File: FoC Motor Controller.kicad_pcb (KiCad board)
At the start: 6 copper layers, 80 x 93.5 mm, 259 parts, among them J1 XT60PW-F, J10 JST_2mm_LiPo, J11 Conn_ARM_SWD_TagConnect_TC203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, J2 XT60PW-M, J3 SM07B-GHS-TB, J6 Conn_01x03, J7 1054301103, J8 1054301103, J9 USB_C_Receptacle_USB2.0_16P, Q1 IPT015N10N5, Q2 IPT015N10N5, Q3 IPT015N10N5, Q4 IPT015N10N5, Q5 IPT015N10N5, Q6 IPT015N10N5, Q7 AO3404A, Q8 AO3404A, SW1 SW_Push_DPDT, U1 LMR38010FDDAR, U2 NCP176AMX330TCG, U3 TPS62172DSG, U4 STM32G431CBT6, U5 DRV8323SRTAR, U6 AS5047P-ATSM, U7 CH340X, U8 TCAN1051HVDR, Y1 CSTNE8M00G520000R0

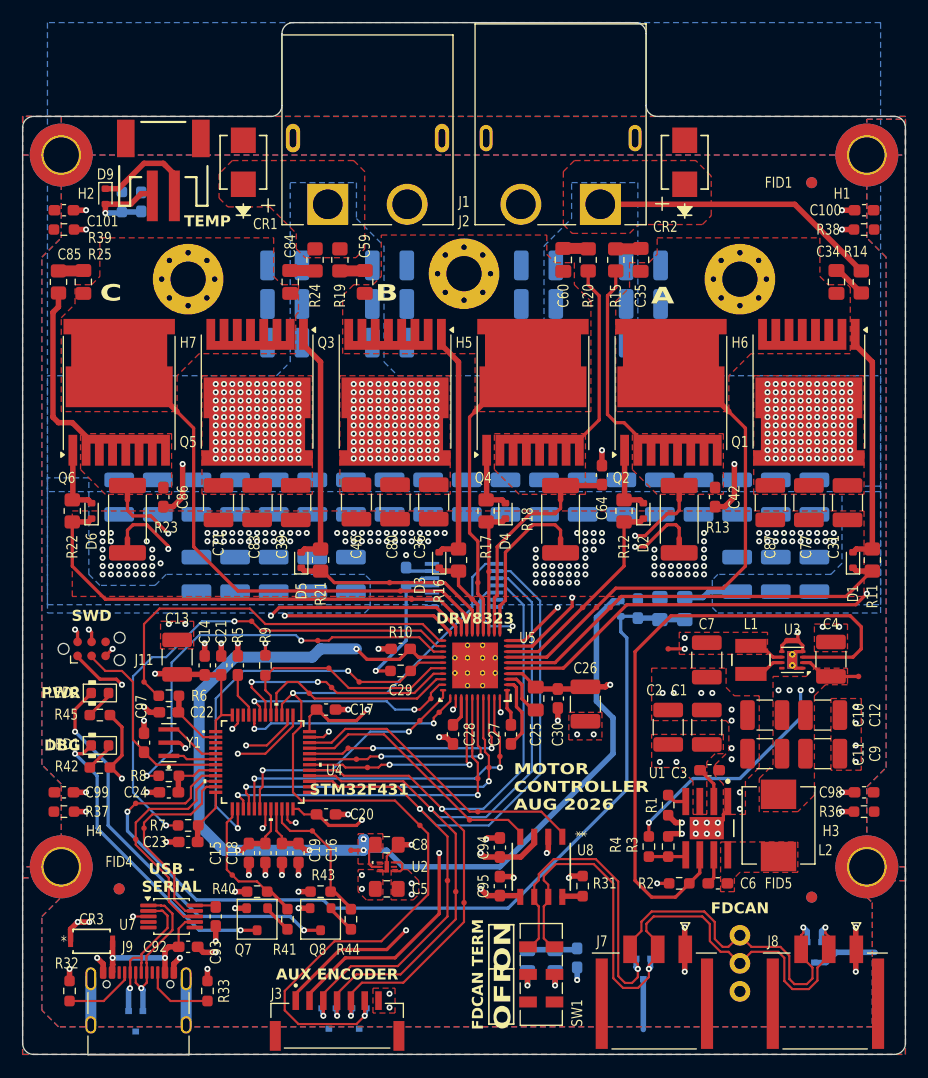
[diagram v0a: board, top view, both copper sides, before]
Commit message: Reorganize project into Altium-style folder structure; add README
- Move hierarchical sheets to Schematics/, lib/ -> Libraries/,
  Manufacturing/ -> Project Outputs/ (BOM, Assembly, Netlist,
  Fabrication, PDF), LTspice benches -> Simulation/
- Update Sheetfile, ${KIPRJMOD} library/3D-model, and output paths
- Drop unused sheets, datasheets, templates and KiCad local history
  from the tracked tree (kept locally, now in .gitignore)
- README.md is the design build log

Co-Authored-By: Claude Sonnet 5 <noreply@anthropic.com>
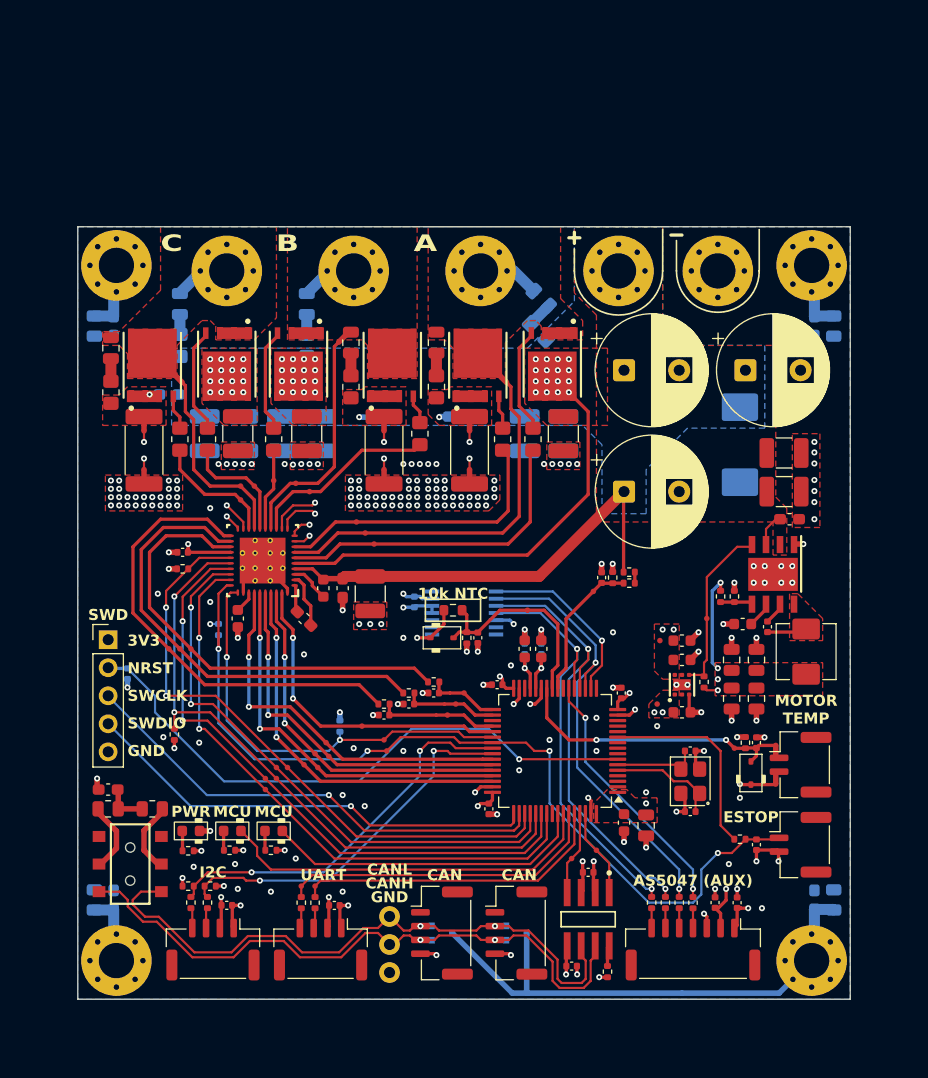
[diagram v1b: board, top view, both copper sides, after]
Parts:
- removed C100, C101: 1n X7R 1kV, Capacitor_SMD:C_0603_1608Metric_Pad1.08x0.95mm_HandSolder
- removed the C13 at (127.5, 89.0)
- removed the C14 at (130.0, 89.8)
- removed the C25 at (160.0, 92.8)
- removed the C26 at (164.5, 93.2)
- removed the C32 at (174.8, 74.5)
- removed the C33 at (178.2, 74.5)
- removed the C4 at (186.8, 89.2)
- removed the C5 at (146.5, 110.0)
- removed C53, C54, C55, C63, C69, C71, C82, C83, C87: 10u X7R 100V, Capacitor_SMD:C_1210_3225Metric_Pad1.33x2.70mm_HandSolder
- removed the C60 at (162.5, 53.0)
- removed C64, C86, C88, C90, C91, C92, C93, C94: 100n X7R 100V, Capacitor_SMD:C_0603_1608Metric_Pad1.08x0.95mm_HandSolder
- removed the C65 at (160.2, 53.5)
- removed the C67 at (137.2, 57.0)
- removed the C68 at (160.8, 74.5)
- removed the C73 at (178.2, 81.5)
- removed the C74 at (157.2, 74.5)
- removed C8: 1u X7R 25V, Capacitor_SMD:C_0805_2012Metric_Pad1.18x1.45mm_HandSolder
- removed C84, C85: 2n2 X7R 100V, Capacitor_SMD:C_0805_2012Metric_Pad1.18x1.45mm_HandSolder
- removed CR1, CR2: SMBJ58CA, SMBJ58CA:SMB
- removed CR3: SM5817PL-TP, SM5817PL-TP:CR_5817PL-TP_MCC
- removed D11, D13, D14: PESD2CANFD24V-UX, PESD2CANFD24V-UX:TVS_PESD2CANFD24V-UX
- removed D2, D3, D5, D6, D8, D9: 1N4148WT, Diode_SMD:D_SOD-523
- removed the D4 at (157.2, 75.8)
- removed the D7 at (167.7, 84.6)
- removed FID1, FID2, FID3, FID4, FID5, FID6: Fiducial, Fiducial:Fiducial_1mm_Mask3mm
- removed the H5 at (153.5, 54.2)
- removed the H6 at (178.5, 54.8)
- removed the H7 at (128.5, 54.8)
- removed the J2 at (162.2, 42.0)
- removed J8: 1054301103, Nano_Fit_1054301103:MOLEX_1054301103
- removed J9: USB_C_Receptacle_USB2.0_16P, Connector_USB:USB_C_Receptacle_XKB_U262-16XN-4BVC11
- removed L1: 2u2, XFL3012-222MEC:IND_XFL3012_COC
- removed LED2: LED_0603_Green, PCM_LED_SMD_AKL:LED_0603_1608Metric
- removed the NT1 at (183.2, 87.5)
- removed NT12, NT13: NetTie_2, NetTie:NetTie-2_SMD_Pad0.5mm
- removed the NT4 at (177.1, 66.4)
- removed the NT7 at (154.9, 66.4)
- removed Q1, Q2: IPT015N10N5, Package_TO_SOT_SMD:Infineon_PG-HSOF-8-1
- removed R1: 64.9k 1%, Resistor_SMD:R_0603_1608Metric_Pad0.98x0.95mm_HandSolder
- removed the R11 at (190.5, 80.2)
- removed the R12 at (168.0, 75.8)
- removed the R14 at (189.5, 55.0)
- removed the R15 at (167.2, 53.0)
- removed the R17 at (155.5, 75.8)
- removed the R22 at (118.0, 75.8)
- removed the R32 at (117.8, 119.3)
- removed the R40 at (134.8, 110.2)
- removed R43: 100k 1%, Resistor_SMD:R_0603_1608Metric_Pad0.98x0.95mm_HandSolder
- removed R5: 10k 1%, Capacitor_SMD:C_0603_1608Metric_Pad1.08x0.95mm_HandSolder
- removed TP1, TP10, TP2, TP3, TP4, TP5, TP8: TestPoint, PCM_SparkFun-Connector:TestPoint-0.5mm
- removed U2: NCP176AMX330TCG, NCP176AMX330TCG:XDFN6_711AT_ONS
- removed U4: STM32G431CBT6, stm32g431cbt6:LQFP48-7x7mm
- removed the U6 at (153.5, 82.5)
- removed Y1: CSTNE8M00G520000R0, CSTNE8M00G520000R0:OSC_CSTNE8M00G520000R0
- added C10: 1u X5R 25V, Capacitor_SMD:C_0603_1608Metric, F.Cu at (173.2, 87.5)
- added C22: 100n X7R 50V, Capacitor_SMD:C_0402_1005Metric, B.Cu at (159.0, 88.2)
- added C23: 100n X7R 50V, Capacitor_SMD:C_0402_1005Metric, F.Cu at (155.8, 102.8)
- added C24: 1u X5R 25V, Capacitor_SMD:C_0603_1608Metric, F.Cu at (168.0, 104.0)
- added C29: 12pF 50V C0G, Capacitor_SMD:C_0402_1005Metric, F.Cu at (174.0, 103.0)
- added DZ2: MM3Z3V3ST, PCM_Diode_SMD_AKL:D_SOD-323, F.Cu at (151.5, 87.2)
- added DZ3: MM3Z3V3ST, PCM_Diode_SMD_AKL:D_SOD-323, F.Cu at (179.5, 99.5)
- added H1: Phase, MountingHole:MountingHole_3.2mm_M3_Pad_Via, F.Cu at (155.0, 54.0)
- added H2: Phase, MountingHole:MountingHole_3.2mm_M3_Pad_Via, F.Cu at (143.5, 54.0)
- added H3: Phase, MountingHole:MountingHole_3.2mm_M3_Pad_Via, F.Cu at (132.0, 54.0)
- added H8: Power, MountingHole:MountingHole_3.2mm_M3_Pad_Via, F.Cu at (167.5, 54.0)
- added H9: Power, MountingHole:MountingHole_3.2mm_M3_Pad_Via, F.Cu at (176.5, 54.0)
- added J4: Conn_01x04_MountingPin, Connector_JST:JST_GH_BM04B-GHS-TBT_1x04-1MP_P1.25mm_Vertical, F.Cu at (151.5, 114.0)
- added J5: Conn_01x04_MountingPin, Connector_JST:JST_GH_BM04B-GHS-TBT_1x04-1MP_P1.25mm_Vertical, F.Cu at (158.2, 114.0)
- added J6: Conn_01x07_MountingPin, Connector_JST:JST_GH_BM07B-GHS-TBT_1x07-1MP_P1.25mm_Vertical, F.Cu at (174.2, 115.5)
- added LED3: LED_0603_Amber, PCM_LED_SMD_AKL:LED_0603_1608Metric, F.Cu at (136.2, 104.8)
- added LED4: LED_0603_Amber, PCM_LED_SMD_AKL:LED_0603_1608Metric, F.Cu at (128.8, 104.8)
- added NT3: NetTie_2, NetTie:NetTie-2_SMD_Pad0.5mm, F.Cu at (157.0, 63.8)
- added NT6: NetTie_2, NetTie:NetTie-2_SMD_Pad0.5mm, F.Cu at (142.5, 60.1)
- added NT9: NetTie_2, NetTie:NetTie-2_SMD_Pad0.5mm, F.Cu at (127.6, 63.8)
- added R23: 3R9 1% 1/8W, Resistor_SMD:R_0805_2012Metric_Pad1.20x1.40mm_HandSolder, B.Cu at (160.2, 59.5)
- added R31: 0R 1% 1/8W, Resistor_SMD:R_0805_2012Metric_Pad1.20x1.40mm_HandSolder, F.Cu at (127.8, 69.2)
- added R34: 3R9 1% 1/8W, Resistor_SMD:R_0805_2012Metric_Pad1.20x1.40mm_HandSolder, F.Cu at (121.5, 65.0)
- added R37: 10k NTC, PCM_SparkFun-Resistor:R_0603_1608Metric, F.Cu at (152.5, 84.8)
- added R42: 2k 1%, Resistor_SMD:R_0402_1005Metric, F.Cu at (130.5, 109.8)
- added R47: 100R 1%, Resistor_SMD:R_0402_1005Metric, F.Cu at (174.2, 111.2)
- added R48: 100R 1%, Resistor_SMD:R_0402_1005Metric, F.Cu at (130.2, 111.2)
- added R49: 100R 1%, Resistor_SMD:R_0402_1005Metric, F.Cu at (173.0, 111.2)
- added R50: 100R 1%, Resistor_SMD:R_0402_1005Metric, F.Cu at (128.8, 111.2)
- added R51: 100R 1%, Resistor_SMD:R_0402_1005Metric, F.Cu at (171.8, 111.2)
- added R52: 100R 1%, Resistor_SMD:R_0402_1005Metric, F.Cu at (140.0, 111.2)
- added R53: 100R 1%, Resistor_SMD:R_0402_1005Metric, F.Cu at (170.5, 111.2)
- added R54: 100R 1%, Resistor_SMD:R_0402_1005Metric, F.Cu at (138.8, 111.2)
- added R58: 0R 1% 1/8W, Resistor_SMD:R_0805_2012Metric, B.Cu at (187.0, 111.0)
- added R59: 0R 1% 1/8W, Resistor_SMD:R_0805_2012Metric, B.Cu at (120.0, 111.0)
- added R66: 1k 1%, Resistor_SMD:R_0402_1005Metric, F.Cu at (128.5, 106.5)
- added R72: 24.9k 1%, Resistor_SMD:R_0402_1005Metric, F.Cu at (168.5, 81.3)
- added R73: 12.4k 1%, Resistor_SMD:R_0402_1005Metric, F.Cu at (168.5, 82.3)
- added TP40: TestPoint, PCM_SparkFun-Connector:TestPoint-0.5mm, F.Cu at (136.2, 73.0)
- added TP41: TestPoint, PCM_SparkFun-Connector:TestPoint-0.5mm, F.Cu at (138.2, 73.2)
- added TP42: TestPoint, PCM_SparkFun-Connector:TestPoint-0.5mm, F.Cu at (139.5, 74.0)
- added TP43: TestPoint, PCM_SparkFun-Connector:TestPoint-0.5mm, F.Cu at (134.5, 73.5)
- added TP44: TestPoint, PCM_SparkFun-Connector:TestPoint-0.5mm, F.Cu at (133.2, 73.5)
- added TP45: TestPoint, PCM_SparkFun-Connector:TestPoint-0.5mm, F.Cu at (133.2, 74.8)
- added U5: STM32G431RBTx, Package_QFP:LQFP-64_10x10mm_P0.5mm, F.Cu at (161.8, 97.5)
- added X1: SMD3225-4, PCM_Crystal_AKL:Crystal_SMD_3225-4Pin_3.2x2.5mm, F.Cu at (174.0, 100.2)
- C11: renamed from C9; value 22u X7R 25V -> 22u X5R 16V; footprint Capacitor_SMD:C_1210_3225Metric_Pad1.33x2.70mm_HandSolder -> Capacitor_SMD:C_0805_2012Metric
- C12: renamed from C10; value 22u X7R 25V -> 22u X5R 16V; footprint Capacitor_SMD:C_1210_3225Metric_Pad1.33x2.70mm_HandSolder -> Capacitor_SMD:C_0805_2012Metric
- C13: renamed from C11; value 22u X7R 25V -> 22u X5R 16V; footprint Capacitor_SMD:C_1210_3225Metric_Pad1.33x2.70mm_HandSolder -> Capacitor_SMD:C_0805_2012Metric
- C14: renamed from C12; value 22u X7R 25V -> 22u X5R 16V; footprint Capacitor_SMD:C_1210_3225Metric_Pad1.33x2.70mm_HandSolder -> Capacitor_SMD:C_0805_2012Metric
- C15, C20: value 1u X7R 25V -> 1u X5R 25V; footprint Capacitor_SMD:C_0603_1608Metric_Pad1.08x0.95mm_HandSolder -> Capacitor_SMD:C_0603_1608Metric
- C16: value 1u X7R 25V -> 22u X5R 16V; footprint Capacitor_SMD:C_0603_1608Metric_Pad1.08x0.95mm_HandSolder -> Capacitor_SMD:C_0805_2012Metric
- C17: value 100n X7R 100V -> 1u X5R 25V; footprint Capacitor_SMD:C_0603_1608Metric_Pad1.08x0.95mm_HandSolder -> Capacitor_SMD:C_0603_1608Metric
- C18, C21: value 100n X7R 100V -> 100n X7R 50V; footprint Capacitor_SMD:C_0603_1608Metric_Pad1.08x0.95mm_HandSolder -> Capacitor_SMD:C_0402_1005Metric
- C19: value 100n X7R 100V -> 100n X7R 50V; footprint Capacitor_SMD:C_0603_1608Metric_Pad1.08x0.95mm_HandSolder -> Capacitor_SMD:C_0402_1005Metric; moved to B.Cu
- C25: renamed from C22; value 2n2 X7R 100V -> 2n2 X7R 50V; footprint Capacitor_SMD:C_0603_1608Metric_Pad1.08x0.95mm_HandSolder -> Capacitor_SMD:C_0402_1005Metric
- C26: renamed from C23; value 2n2 X7R 100V -> 2n2 X7R 50V; footprint Capacitor_SMD:C_0603_1608Metric_Pad1.08x0.95mm_HandSolder -> Capacitor_SMD:C_0402_1005Metric
- C27: renamed from C24; value 2n2 X7R 100V -> 2n2 X7R 50V; footprint Capacitor_SMD:C_0603_1608Metric_Pad1.08x0.95mm_HandSolder -> Capacitor_SMD:C_0402_1005Metric
- C28: value 1u X7R 6V3 -> 12pF 50V C0G; footprint Capacitor_SMD:C_0603_1608Metric_Pad1.08x0.95mm_HandSolder -> Capacitor_SMD:C_0402_1005Metric
- C31: value 10u X7R 100V -> 1u X5R 25V; footprint Capacitor_SMD:C_1210_3225Metric_Pad1.33x2.70mm_HandSolder -> Capacitor_SMD:C_0603_1608Metric
- C32: renamed from C29; value 100n X7R 100V -> 100n X7R 50V; footprint Capacitor_SMD:C_0603_1608Metric_Pad1.08x0.95mm_HandSolder -> Capacitor_SMD:C_0402_1005Metric
- C34: value 2n2 X7R 100V -> 100uF 100V; footprint Capacitor_SMD:C_0805_2012Metric_Pad1.18x1.45mm_HandSolder -> Capacitor_THT:CP_Radial_D10.0mm_P5.00mm
- C35: footprint Capacitor_SMD:C_0805_2012Metric_Pad1.18x1.45mm_HandSolder -> Capacitor_SMD:C_0805_2012Metric; moved to B.Cu
- C36, C45, C46, C56: value 10u X7R 100V -> 2n2 X7R 100V; footprint Capacitor_SMD:C_1210_3225Metric_Pad1.33x2.70mm_HandSolder -> Capacitor_SMD:C_0805_2012Metric
- C37: value 10u X7R 100V -> 100uF 100V; footprint Capacitor_SMD:C_1210_3225Metric_Pad1.33x2.70mm_HandSolder -> Capacitor_THT:CP_Radial_D10.0mm_P5.00mm; moved to F.Cu
- C38, C49, C58: value 10u X7R 100V -> 100n X7R 100V; footprint Capacitor_SMD:C_1210_3225Metric_Pad1.33x2.70mm_HandSolder -> Capacitor_SMD:C_0603_1608Metric_Pad1.08x0.95mm_HandSolder
- C39: value 10u X7R 100V -> 100uF 100V; footprint Capacitor_SMD:C_1210_3225Metric_Pad1.33x2.70mm_HandSolder -> Capacitor_THT:CP_Radial_D10.0mm_P5.00mm
- C40, C51: value 10u X7R 100V -> 4u7 X7R 100V; moved to F.Cu
- C41, C79: value 10u X7R 100V -> 1u X5R 25V; footprint Capacitor_SMD:C_1210_3225Metric_Pad1.33x2.70mm_HandSolder -> Capacitor_SMD:C_0603_1608Metric; moved to F.Cu
- C42: value 100n X7R 100V -> 2n2 X7R 50V; footprint Capacitor_SMD:C_0603_1608Metric_Pad1.08x0.95mm_HandSolder -> Capacitor_SMD:C_0402_1005Metric
- C43, C44, C47, C48, C50, C52, C80: value 10u X7R 100V -> 4u7 X7R 100V
- C57: value 10u X7R 100V -> 2n2 X7R 100V; footprint Capacitor_SMD:C_1210_3225Metric_Pad1.33x2.70mm_HandSolder -> Capacitor_SMD:C_0805_2012Metric; moved to F.Cu
- C59: value 2n2 X7R 100V -> 4u7 X7R 100V; footprint Capacitor_SMD:C_0805_2012Metric_Pad1.18x1.45mm_HandSolder -> Capacitor_SMD:C_1210_3225Metric_Pad1.33x2.70mm_HandSolder
- C60: renamed from C89; value 100n X7R 100V -> 100n X7R 50V; footprint Capacitor_SMD:C_0603_1608Metric_Pad1.08x0.95mm_HandSolder -> Capacitor_SMD:C_0402_1005Metric; moved to F.Cu
- C61, C62, C70, C72, C78, C81: value 10u X7R 100V -> 100n X7R 50V; footprint Capacitor_SMD:C_1210_3225Metric_Pad1.33x2.70mm_HandSolder -> Capacitor_SMD:C_0402_1005Metric; moved to F.Cu
- C65: renamed from C95; value 100n X7R 100V -> 100n X7R 50V; footprint Capacitor_SMD:C_0603_1608Metric_Pad1.08x0.95mm_HandSolder -> Capacitor_SMD:C_0402_1005Metric
- C66, C77: value 10u X7R 100V -> 100n X7R 50V; footprint Capacitor_SMD:C_1210_3225Metric_Pad1.33x2.70mm_HandSolder -> Capacitor_SMD:C_0402_1005Metric
- C67: renamed from C97; value 100n X7R 100V -> 100n X7R 50V; footprint Capacitor_SMD:C_0603_1608Metric_Pad1.08x0.95mm_HandSolder -> Capacitor_SMD:C_0402_1005Metric; moved to B.Cu
- C68: renamed from C96; moved to F.Cu
- C7: value 22u X7R 25V -> 1u X5R 25V; footprint Capacitor_SMD:C_1210_3225Metric_Pad1.33x2.70mm_HandSolder -> Capacitor_SMD:C_0603_1608Metric
- C73: renamed from C98; moved to B.Cu
- C74: renamed from C99; moved to B.Cu
- C75, C76: value 10u X7R 100V -> 1n X7R 1kV; footprint Capacitor_SMD:C_1210_3225Metric_Pad1.33x2.70mm_HandSolder -> Capacitor_SMD:C_0603_1608Metric_Pad1.08x0.95mm_HandSolder
- C9: renamed from C6; value 100n X7R 100V -> 100n X7R 50V; footprint Capacitor_SMD:C_0603_1608Metric_Pad1.08x0.95mm_HandSolder -> Capacitor_SMD:C_0402_1005Metric
- D1: value 1N4148WT -> SMCJ51CA; footprint Diode_SMD:D_SOD-523 -> PCM_Diode_SMD_AKL:D_SMC_TVS; moved to B.Cu
- D4: renamed from D10; value PESD2CANFD24V-UX -> PESD2CANFD24V-K
- D7: renamed from D12; value PESD2CANFD24V-UX -> PESD2CANFD24V-K
- H4: renamed from H1; value MountingHole_Pad -> M3_MountingHole_Pad; footprint MountingHole:MountingHole_3.2mm_M3_ISO7380_Pad_TopBottom -> MountingHole:MountingHole_3.2mm_M3_Pad_Via
- H5: renamed from H2; value MountingHole_Pad -> M3_MountingHole_Pad; footprint MountingHole:MountingHole_3.2mm_M3_ISO7380_Pad_TopBottom -> MountingHole:MountingHole_3.2mm_M3_Pad_Via
- H6: renamed from H3; value MountingHole_Pad -> M3_MountingHole_Pad; footprint MountingHole:MountingHole_3.2mm_M3_ISO7380_Pad_TopBottom -> MountingHole:MountingHole_3.2mm_M3_Pad_Via
- H7: renamed from H4; value MountingHole_Pad -> M3_MountingHole_Pad; footprint MountingHole:MountingHole_3.2mm_M3_ISO7380_Pad_TopBottom -> MountingHole:MountingHole_3.2mm_M3_Pad_Via
- J1: value XT60PW-F -> Conn_01x04_MountingPin; footprint XT60PW-F:AMASS_XT60PW-F -> Connector_JST:JST_GH_BM04B-GHS-TBT_1x04-1MP_P1.25mm_Vertical
- J10: value JST_2mm_LiPo -> Conn_01x02_MountingPin; footprint PCM_SparkFun-Connector:JST_1x02_P2.0mm_Horizontal_SMD -> Connector_JST:JST_GH_BM02B-GHS-TBT_1x02-1MP_P1.25mm_Vertical
- J11: value Conn_ARM_SWD_TagConnect_TC2030-NL -> Conn_01x02_MountingPin; footprint Connector:Tag-Connect_TC2030-IDC-NL_2x03_P1.27mm_Vertical -> Connector_JST:JST_GH_BM02B-GHS-TBT_1x02-1MP_P1.25mm_Vertical
- J2: renamed from J6; moved to F.Cu
- J3: value SM07B-GHS-TB -> Conn_01x04_MountingPin; footprint SM07B_GHS_TB:JST_SM07B-GHS-TB -> Connector_JST:JST_GH_BM04B-GHS-TBT_1x04-1MP_P1.25mm_Vertical
- J7: value 1054301103 -> Conn_01x05; footprint Nano_Fit_1054301103:MOLEX_1054301103 -> Connector_PinHeader_2.54mm:PinHeader_1x05_P2.54mm_Vertical
- L2: value 3u3 -> 10uH 125mΩ 3.2A; footprint FXL0630-330-M:INDM7066X300N -> Inductor_SMD:L_Changjiang_FXL0530
- NT11: moved to F.Cu
- Q3, Q4, Q5, Q6: value IPT015N10N5 -> ISC030N10NM6; footprint Package_TO_SOT_SMD:Infineon_PG-HSOF-8-1 -> ISC030N10NM6:IFX-PG-TDSON-8-36-V
- Q7, Q8: value AO3404A -> ISC030N10NM6; footprint PCM_Package_TO_SOT_SMD_AKL:SOT-23 -> ISC030N10NM6:IFX-PG-TDSON-8-36-V
- R10: renamed from R4; footprint Resistor_SMD:R_0603_1608Metric_Pad0.98x0.95mm_HandSolder -> Resistor_SMD:R_0402_1005Metric
- R11: renamed from R2; footprint Resistor_SMD:R_0603_1608Metric_Pad0.98x0.95mm_HandSolder -> Resistor_SMD:R_0402_1005Metric
- R12: renamed from R3; footprint Resistor_SMD:R_0603_1608Metric_Pad0.98x0.95mm_HandSolder -> Resistor_SMD:R_0402_1005Metric
- R13: renamed from R6; footprint Resistor_SMD:R_0603_1608Metric_Pad0.98x0.95mm_HandSolder -> Resistor_SMD:R_0402_1005Metric
- R14: renamed from R7; footprint Resistor_SMD:R_0603_1608Metric_Pad0.98x0.95mm_HandSolder -> Resistor_SMD:R_0402_1005Metric
- R15: renamed from R8; footprint Resistor_SMD:R_0603_1608Metric_Pad0.98x0.95mm_HandSolder -> Resistor_SMD:R_0402_1005Metric
- R16, R19: value 3R9 1% 1/8W -> 100k 1%; footprint Resistor_SMD:R_0805_2012Metric_Pad1.20x1.40mm_HandSolder -> Resistor_SMD:R_0402_1005Metric; moved to B.Cu
- R17: renamed from R9; footprint Resistor_SMD:R_0603_1608Metric_Pad0.98x0.95mm_HandSolder -> Resistor_SMD:R_0402_1005Metric
- R18: renamed from R10; footprint Resistor_SMD:R_0603_1608Metric_Pad0.98x0.95mm_HandSolder -> Resistor_SMD:R_0402_1005Metric
- R20, R21, R25: value 3R9 1% 1/8W -> 0R 1% 1/8W
- R22: renamed from R13; value 5mΩ 3W 1% -> 3mΩ 3W 1%
- R26: value 39k 1% 1/8W -> 0R 1% 1/8W; moved to F.Cu
- R27: renamed from R18; value 5mΩ 3W 1% -> 3mΩ 3W 1%
- R28: value 10k -> 3R9 1% 1/8W; footprint PCM_SparkFun-Resistor:R_0603_1608Metric -> Resistor_SMD:R_0805_2012Metric_Pad1.20x1.40mm_HandSolder
- R29: value 10k 1% -> 3R9 1% 1/8W; footprint Resistor_SMD:R_0603_1608Metric_Pad0.98x0.95mm_HandSolder -> Resistor_SMD:R_0805_2012Metric_Pad1.20x1.40mm_HandSolder; moved to F.Cu
- R30: value 2k 1% -> 0R 1% 1/8W; footprint Resistor_SMD:R_0603_1608Metric_Pad0.98x0.95mm_HandSolder -> Resistor_SMD:R_0805_2012Metric_Pad1.20x1.40mm_HandSolder; moved to F.Cu
- R32: renamed from R23; value 5mΩ 3W 1% -> 3mΩ 3W 1%
- R33: value 5k1 1% -> 3R9 1% 1/8W; footprint Resistor_SMD:R_0603_1608Metric_Pad0.98x0.95mm_HandSolder -> Resistor_SMD:R_0805_2012Metric_Pad1.20x1.40mm_HandSolder; moved to B.Cu
- R36: renamed from R27; value 2k2 1% 1/8W -> 2k 1%; footprint Resistor_SMD:R_0805_2012Metric_Pad1.20x1.40mm_HandSolder -> Resistor_SMD:R_0402_1005Metric; moved to F.Cu
- R38: value 0R -> 10k 1%; footprint Resistor_SMD:R_0603_1608Metric_Pad0.98x0.95mm_HandSolder -> Resistor_SMD:R_0402_1005Metric
- R39: value 0R -> 2k 1%; footprint Resistor_SMD:R_0603_1608Metric_Pad0.98x0.95mm_HandSolder -> Resistor_SMD:R_0402_1005Metric
- R40: renamed from R31; footprint Resistor_SMD:R_0603_1608Metric_Pad0.98x0.95mm_HandSolder -> Resistor_SMD:R_0402_1005Metric
- R41: value 100R 1% 1/10W -> 1k 1%; footprint Resistor_SMD:R_0603_1608Metric_Pad0.98x0.95mm_HandSolder -> Resistor_SMD:R_0402_1005Metric
- R44: value 100R 1% 1/10W -> 2k 1%; footprint Resistor_SMD:R_0603_1608Metric_Pad0.98x0.95mm_HandSolder -> Resistor_SMD:R_0402_1005Metric
- R45: renamed from R34; value 60R4 1% 1/8W -> 60R4 1%; footprint Resistor_SMD:R_0805_2012Metric_Pad1.20x1.40mm_HandSolder -> Resistor_SMD:R_0805_2012Metric; moved to F.Cu
- R46: renamed from R35; value 60R4 1% 1/8W -> 60R4 1%; footprint Resistor_SMD:R_0805_2012Metric_Pad1.20x1.40mm_HandSolder -> Resistor_SMD:R_0805_2012Metric; moved to F.Cu
- R56: renamed from R36; value 0R -> 0R 1% 1/8W; footprint Resistor_SMD:R_0603_1608Metric_Pad0.98x0.95mm_HandSolder -> Resistor_SMD:R_0805_2012Metric; moved to B.Cu
- R57: renamed from R37; value 0R -> 0R 1% 1/8W; footprint Resistor_SMD:R_0603_1608Metric_Pad0.98x0.95mm_HandSolder -> Resistor_SMD:R_0805_2012Metric; moved to B.Cu
- R62: renamed from R42; value 100R 1% 1/10W -> 1k 1%; footprint Resistor_SMD:R_0603_1608Metric_Pad0.98x0.95mm_HandSolder -> Resistor_SMD:R_0402_1005Metric
- R65: renamed from R45; value 100R 1% 1/10W -> 1k 1%; footprint Resistor_SMD:R_0603_1608Metric_Pad0.98x0.95mm_HandSolder -> Resistor_SMD:R_0402_1005Metric
- SW1: footprint Button_Switch_SMD:SW_DPDT_CK_JS202011JCQN -> PCM_SparkFun-Switch:Slide_DPDT_SMD_7.2x3.5mm
- U1: value LMR38010FDDAR -> AS5047P-ATSM; footprint LMR38010FDDAR:DDA0008E-IPC_A -> AS5047P:TSSOP14_OSM; moved to B.Cu
- U3: value TPS62172DSG -> LMR36520ADDAR; footprint Package_SON:WSON-8-1EP_2x2mm_P0.5mm_EP0.9x1.6mm_ThermalVias -> LMR36520ADDAR:DDA0008J
- U7: value CH340X -> TLV75733PDRV; footprint Package_SO:MSOP-10_3x3mm_P0.5mm -> PCM_SparkFun-Semiconductor-Standard:WDFN-6_2x2mm
- U8: value TCAN1051HVDR -> TCAN1044AVDRQ1; footprint TCAN1051HVDR:D8_TEX -> ul_TCAN1044AVDRQ1:D0008A-IPC_A
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- renumbered C27 to C30, C30 to C33, C1 to C4, C2 to C5, C3 to C6, NT2 to NT1, NT3 to NT2, NT5 to NT4, NT6 to NT5, NT8 to NT7, NT9 to NT8, U5 to U6
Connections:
- C15 pad 1: +A3V3 -> +3V3
- C16 pad 1: +A3V3 -> +3V3
- C18 pad 1: +A3V3 -> +3V3
- C19 pad 1: +A3V3 -> +3V3
- C28 pad 1: /Project Architecture/Motor Control - Driver/DVDD -> /Project Architecture/MCU - IOs/OSC_OUT
- C31 pad 1: +VBAT -> /Project Architecture/Motor Control - Driver/DVDD
- C32 pad 1: +A3V3 -> +3V3
- C33 pad 1: +VBAT -> +VPROT
- C34 pad 1: Net-(C34-Pad1) -> +VPROT
- C34 pad 2: /Project Architecture/Motor Control - Driver/MOSFETs/OUT_A -> GND
- C35 pad 1: /Project Architecture/Motor Control - Driver/MOSFETs/OUT_A -> Net-(C35-Pad1)
- C35 pad 2: Net-(C35-Pad2) -> /Project Architecture/Motor Control - Driver/MOSFETs/OUT_A
- C36 pad 1: +VBAT -> /Project Architecture/Motor Control - Driver/MOSFETs/OUT_A
- C36 pad 2: GND -> Net-(C36-Pad2)
- C37 pad 1: +VBAT -> +VPROT
- C38 pad 1: +VBAT -> +VPROT
- C38 pad 2: GND -> /Project Architecture/Motor Control - Driver/MOSFETs/SOURCE_A
- C39 pad 1: +VBAT -> +VPROT
- C4 pad 1: +VBAT -> +VPROT
- C40 pad 1: +VBAT -> +VPROT
- C41 pad 1: +VBAT -> +5V
- C42 pad 1: +VBAT -> /Project Architecture/MCU - IOs/DRV_ENABLE
- C42 pad 2: /Project Architecture/Motor Control - Driver/MOSFETs/SOURCE_A -> GND
- C43 pad 1: +VBAT -> +VPROT
- C44 pad 1: +VBAT -> +VPROT
- C45 pad 1: +VBAT -> Net-(C45-Pad1)
- C45 pad 2: GND -> /Project Architecture/Motor Control - Driver/MOSFETs/OUT_B
- C46 pad 1: +VBAT -> /Project Architecture/Motor Control - Driver/MOSFETs/OUT_B
- C46 pad 2: GND -> Net-(C46-Pad2)
- C47 pad 1: +VBAT -> +VPROT
- C48 pad 1: +VBAT -> +VPROT
- C49 pad 1: +VBAT -> +VPROT
- C49 pad 2: GND -> /Project Architecture/Motor Control - Driver/MOSFETs/SOURCE_B
- C5 pad 1: +VBAT -> +VPROT
- C50 pad 1: +VBAT -> +VPROT
- C51 pad 1: +VBAT -> +VPROT
- C52 pad 1: +VBAT -> +VPROT
- C56 pad 1: +VBAT -> Net-(C56-Pad1)
- C56 pad 2: GND -> /Project Architecture/Motor Control - Driver/MOSFETs/OUT_C
- C57 pad 1: +VBAT -> /Project Architecture/Motor Control - Driver/MOSFETs/OUT_C
- C57 pad 2: GND -> Net-(C57-Pad2)
- C58 pad 1: +VBAT -> +VPROT
- C58 pad 2: GND -> /Project Architecture/Motor Control - Driver/MOSFETs/SOURCE_C
- C59 pad 1: Net-(C59-Pad1) -> +VPROT
- C59 pad 2: /Project Architecture/Motor Control - Driver/MOSFETs/OUT_B -> GND
- C6 pad 1: +VBAT -> +VPROT
- C61 pad 1: +VBAT -> /Project Architecture/MCU - IOs/TEMP_SENSE
- C62 pad 1: +VBAT -> /Project Architecture/MCU - IOs/MOT_TEMP_SENSE
- C66 pad 1: +VBAT -> +3V3
- C7 pad 1: +3V3 -> Net-(U3-VCC)
- C70 pad 1: +VBAT -> +5V
- C72 pad 1: +VBAT -> +3V3
- C73 pad 1: CHASSIS -> CHASSIS1
- C74 pad 1: CHASSIS -> CHASSIS2
- C75 pad 1: +VBAT -> CHASSIS3
- C76 pad 1: +VBAT -> CHASSIS4
- C77 pad 1: +VBAT -> +3V3
- C78 pad 1: +VBAT -> +3V3
- C79 pad 1: +VBAT -> +VPROT
- C79 pad 2: GND -> /Project Architecture/Motor Control - Driver/VCP
- C80 pad 1: +VBAT -> +VPROT
- C81 pad 1: +VBAT -> +3V3
- C9 pad 1: Net-(U1-BOOT) -> Net-(U3-BOOT)
- D1 pad 1: /Project Architecture/Motor Control - Driver/GHA -> GND
- D1 pad 2: /Project Architecture/Motor Control - Driver/MOSFETs/GH_A -> +VPROT
- D4 pad 1: /Project Architecture/Interface - CAN FD/FDCAN_N -> /Project Architecture/Interface - CAN FD/FDCAN_P
- D4 pad 2: /Project Architecture/Interface - CAN FD/FDCAN_P -> /Project Architecture/Interface - CAN FD/FDCAN_N
- D4 pad 3: CHASSIS -> CHASSIS3
- D7 pad 1: /Project Architecture/Interface - CAN FD/FDCAN_N -> /Project Architecture/Interface - CAN FD/FDCAN_P
- D7 pad 2: /Project Architecture/Interface - CAN FD/FDCAN_P -> /Project Architecture/Interface - CAN FD/FDCAN_N
- D7 pad 3: CHASSIS -> CHASSIS3
- H4 pad 1: CHASSIS -> CHASSIS1
- H5 pad 1: CHASSIS -> CHASSIS2
- H6 pad 1: CHASSIS -> CHASSIS3
- H7 pad 1: CHASSIS -> CHASSIS4
- J1 pad 1: +VBAT -> GND
- J1 pad 2: GND -> +3V3
- J11 pad 1: +3V3 -> /Project Architecture/MCU - IOs/DRV_ENABLE
- J11 pad 2: /Project Architecture/Interface - Interconnects/SWDIO -> GND
- J3 pad 1: +5V -> GND
- J3 pad 3: /Project Architecture/Interface - Interconnects/POS_SENSOR_CLK -> Net-(J3-Pin_3)
- J3 pad 4: /Project Architecture/Interface - Interconnects/POS_SENSOR_MISO -> Net-(J3-Pin_4)
- J7 pad 1: GND -> +3V3
- J7 pad 2: /Project Architecture/Interface - CAN FD/FDCAN_P -> /Project Architecture/Interface - Interconnects/NRST
- J7 pad 3: /Project Architecture/Interface - CAN FD/FDCAN_N -> /Project Architecture/Interface - Interconnects/SWCLK
- LED1 pad 1: /Project Architecture/USER - LEDs/MCU_LED_D -> /Project Architecture/MCU - IOs/MCU_LED
- NT10 pad 1: /Project Architecture/Motor Control - Driver/SHC -> +3V3
- NT10 pad 2: /Project Architecture/Motor Control - Driver/MOSFETs/OUT_C -> /Project Architecture/Interface - Interconnects/MOT_NTC_L
- NT11 pad 1: GND -> /Project Architecture/MCU - IOs/MOT_TEMP_SENSE
- NT11 pad 2: Net-(U6-TEST) -> /Project Architecture/Interface - Interconnects/MOT_NTC_H
- Q3 pad 1: /Project Architecture/Motor Control - Driver/MOSFETs/GH_B -> /Project Architecture/Motor Control - Driver/MOSFETs/OUT_A
- Q3 pad 2: /Project Architecture/Motor Control - Driver/MOSFETs/OUT_B -> /Project Architecture/Motor Control - Driver/MOSFETs/OUT_A
- Q3 pad 3: +VBAT -> /Project Architecture/Motor Control - Driver/MOSFETs/OUT_A
- Q4 pad 1: /Project Architecture/Motor Control - Driver/MOSFETs/GL_B -> /Project Architecture/Motor Control - Driver/MOSFETs/SOURCE_A
- Q4 pad 2: /Project Architecture/Motor Control - Driver/MOSFETs/SOURCE_B -> /Project Architecture/Motor Control - Driver/MOSFETs/SOURCE_A
- Q4 pad 3: /Project Architecture/Motor Control - Driver/MOSFETs/OUT_B -> /Project Architecture/Motor Control - Driver/MOSFETs/SOURCE_A
- Q5 pad 1: /Project Architecture/Motor Control - Driver/MOSFETs/GH_C -> /Project Architecture/Motor Control - Driver/MOSFETs/OUT_B
- Q5 pad 2: /Project Architecture/Motor Control - Driver/MOSFETs/OUT_C -> /Project Architecture/Motor Control - Driver/MOSFETs/OUT_B
- Q5 pad 3: +VBAT -> /Project Architecture/Motor Control - Driver/MOSFETs/OUT_B
- Q6 pad 1: /Project Architecture/Motor Control - Driver/MOSFETs/GL_C -> /Project Architecture/Motor Control - Driver/MOSFETs/SOURCE_B
- Q6 pad 2: /Project Architecture/Motor Control - Driver/MOSFETs/SOURCE_C -> /Project Architecture/Motor Control - Driver/MOSFETs/SOURCE_B
- Q6 pad 3: /Project Architecture/Motor Control - Driver/MOSFETs/OUT_C -> /Project Architecture/Motor Control - Driver/MOSFETs/SOURCE_B
- Q7 pad 1: /Project Architecture/USER - LEDs/MCU_LED_G -> /Project Architecture/Motor Control - Driver/MOSFETs/OUT_C
- Q7 pad 2: GND -> /Project Architecture/Motor Control - Driver/MOSFETs/OUT_C
- Q7 pad 3: /Project Architecture/USER - LEDs/MCU_LED_D -> /Project Architecture/Motor Control - Driver/MOSFETs/OUT_C
- Q8 pad 1: /Project Architecture/USER - LEDs/PWR_LED_G -> /Project Architecture/Motor Control - Driver/MOSFETs/SOURCE_C
- Q8 pad 2: GND -> /Project Architecture/Motor Control - Driver/MOSFETs/SOURCE_C
- Q8 pad 3: /Project Architecture/USER - LEDs/PWR_LED_D -> /Project Architecture/Motor Control - Driver/MOSFETs/SOURCE_C
- R16 pad 1: /Project Architecture/Motor Control - Driver/MOSFETs/GH_B -> /Project Architecture/MCU - IOs/DRV_ENABLE
- R16 pad 2: /Project Architecture/Motor Control - Driver/GHB -> GND
- R19 pad 1: +VBAT -> /Project Architecture/MCU - IOs/DRV_CAL
- R19 pad 2: Net-(C59-Pad1) -> GND
- R20 pad 1: Net-(C60-Pad2) -> /Project Architecture/Motor Control - Driver/MOSFETs/GH_A
- R20 pad 2: /Project Architecture/Motor Control - Driver/MOSFETs/SOURCE_B -> /Project Architecture/Motor Control - Driver/GHA
- R21 pad 1: /Project Architecture/Motor Control - Driver/MOSFETs/GH_C -> /Project Architecture/Motor Control - Driver/MOSFETs/GL_A
- R21 pad 2: /Project Architecture/Motor Control - Driver/GHC -> /Project Architecture/Motor Control - Driver/GLA
- R24 pad 1: +VBAT -> Net-(C36-Pad2)
- R24 pad 2: Net-(C84-Pad1) -> /Project Architecture/Motor Control - Driver/MOSFETs/SOURCE_A
- R25 pad 1: Net-(C85-Pad2) -> /Project Architecture/Motor Control - Driver/MOSFETs/GH_B
- R25 pad 2: /Project Architecture/Motor Control - Driver/MOSFETs/SOURCE_C -> /Project Architecture/Motor Control - Driver/GHB
- R26 pad 1: +VBAT -> /Project Architecture/Motor Control - Driver/MOSFETs/GL_B
- R26 pad 2: /Project Architecture/MCU - IOs/VBAT_SENSE -> /Project Architecture/Motor Control - Driver/GLB
- R28 pad 1: /Project Architecture/MCU - IOs/TEMP_SENSE -> +VPROT
- R28 pad 2: +A3V3 -> Net-(C45-Pad1)
- R29 pad 1: /Project Architecture/MCU - IOs/TEMP_SENSE -> Net-(C46-Pad2)
- R29 pad 2: GND -> /Project Architecture/Motor Control - Driver/MOSFETs/SOURCE_B
- R30 pad 1: /Project Architecture/MCU - IOs/MOT_TEMP_SENSE -> /Project Architecture/Motor Control - Driver/MOSFETs/GH_C
- R30 pad 2: GND -> /Project Architecture/Motor Control - Driver/GHC
- R33 pad 1: /Project Architecture/Interface - Interconnects/CC2 -> +VPROT
- R33 pad 2: GND -> Net-(C56-Pad1)
- R38 pad 1: CHASSIS -> /Project Architecture/MCU - IOs/TEMP_SENSE
- R39 pad 1: CHASSIS -> /Project Architecture/MCU - IOs/MOT_TEMP_SENSE
- R41 pad 1: /Project Architecture/MCU - IOs/MCU_LED -> /Project Architecture/MCU - IOs/DRV_ENABLE
- R41 pad 2: /Project Architecture/USER - LEDs/MCU_LED_G -> /Project Architecture/MCU - IOs/PC3
- R44 pad 1: /Project Architecture/MCU - IOs/PWR_LED -> +3V3
- R44 pad 2: /Project Architecture/USER - LEDs/PWR_LED_G -> /Project Architecture/Interface - Interconnects/I2C3_SCL
- R56 pad 1: CHASSIS -> CHASSIS1
- R57 pad 1: CHASSIS -> CHASSIS2
- R62 pad 1: +5V -> +3V3
- R65 pad 1: +5V -> +3V3
- TP11 pad 1: /Project Architecture/MCU - IOs/PWM_PHASEC_H -> /Project Architecture/Interface - CAN FD/FDCAN_TX
- TP12 pad 1: /Project Architecture/MCU - IOs/PWM_PHASEC_L -> /Project Architecture/Interface - CAN FD/FDCAN_RX
- TP13 pad 1: /Project Architecture/MCU - IOs/SOC -> /Project Architecture/Interface - Interconnects/UART1_TX
- TP14 pad 1: /Project Architecture/MCU - IOs/SOB -> /Project Architecture/Interface - Interconnects/UART1_RX
- TP15 pad 1: /Project Architecture/MCU - IOs/SOA -> /Project Architecture/MCU - IOs/FILTER_SOC
- TP16 pad 1: /Project Architecture/MCU - IOs/DRV_nFAULT -> /Project Architecture/MCU - IOs/FILTER_SOB
- TP17 pad 1: /Project Architecture/MCU - IOs/DRV_ENABLE -> /Project Architecture/MCU - IOs/FILTER_SOA
- TP18 pad 1: /Project Architecture/MCU - IOs/DRV_CAL -> /Project Architecture/MCU - IOs/SOC
- TP19 pad 1: /Project Architecture/Interface - Interconnects/POS_SENSOR_CS -> /Project Architecture/MCU - IOs/SOB
- TP20 pad 1: /Project Architecture/Interface - Interconnects/POS_SENSOR_CLK -> /Project Architecture/MCU - IOs/SOA
- TP21 pad 1: /Project Architecture/Interface - Interconnects/POS_SENSOR_MISO -> /Project Architecture/MCU - IOs/PWM_PHASEA_H
- TP22 pad 1: /Project Architecture/Interface - Interconnects/POS_SENSOR_MOSI -> /Project Architecture/MCU - IOs/PWM_PHASEA_L
- TP23 pad 1: /Project Architecture/MCU - IOs/VBAT_SENSE -> /Project Architecture/MCU - IOs/PWM_PHASEB_H
- TP24 pad 1: /Project Architecture/Interface - USB to UART/LPUART1_TX -> /Project Architecture/MCU - IOs/PWM_PHASEB_L
- TP25 pad 1: /Project Architecture/Interface - USB to UART/LPUART1_RX -> /Project Architecture/MCU - IOs/PWM_PHASEC_H
- TP26 pad 1: /Project Architecture/Interface - CAN FD/FDCAN_TX -> /Project Architecture/MCU - IOs/PWM_PHASEC_L
- TP27 pad 1: /Project Architecture/Interface - CAN FD/FDCAN_RX -> /Project Architecture/MCU - IOs/DRV_nFAULT
- TP28 pad 1: +5V -> /Project Architecture/MCU - IOs/DRV_ENABLE
- TP29 pad 1: +3V3 -> /Project Architecture/MCU - IOs/DRV_CAL
- TP30 pad 1: +A3V3 -> /Project Architecture/MCU - IOs/DRV_MISO
- TP31 pad 1: /Project Architecture/Motor Control - Driver/GHA -> /Project Architecture/MCU - IOs/DRV_MOSI
- TP32 pad 1: /Project Architecture/Motor Control - Driver/SHA -> /Project Architecture/MCU - IOs/DRV_SCLK
- TP33 pad 1: /Project Architecture/Motor Control - Driver/GLA -> /Project Architecture/MCU - IOs/DRV_CS
- TP34 pad 1: /Project Architecture/Motor Control - Driver/GHB -> /Project Architecture/MCU - IOs/VBAT_SENSE
- TP35 pad 1: /Project Architecture/Motor Control - Driver/SHB -> /Project Architecture/MCU - IOs/TEMP_SENSE
- TP36 pad 1: /Project Architecture/Motor Control - Driver/GLB -> /Project Architecture/MCU - IOs/MOT_TEMP_SENSE
- TP37 pad 1: /Project Architecture/Motor Control - Driver/GHC -> /Project Architecture/Motor Control - Driver/GHA
- TP38 pad 1: /Project Architecture/Motor Control - Driver/SHC -> /Project Architecture/Motor Control - Driver/SHA
- TP39 pad 1: /Project Architecture/Motor Control - Driver/GLC -> /Project Architecture/Motor Control - Driver/GLA
- TP6 pad 1: /Project Architecture/MCU - IOs/DRV_CS -> /Project Architecture/Power - Generation/PG_5V
- TP7 pad 1: /Project Architecture/MCU - IOs/PWM_PHASEA_H -> +5V
- TP9 pad 1: /Project Architecture/MCU - IOs/PWM_PHASEB_H -> +3V3
- U1 pad 1: GND -> /Project Architecture/Interface - Interconnects/POS_SENSOR_CS
- U1 pad 2: +VBAT -> /Project Architecture/Interface - Interconnects/POS_SENSOR_CLK
- U1 pad 3: +VBAT -> /Project Architecture/Interface - Interconnects/POS_SENSOR_MISO
- U1 pad 4: /Project Architecture/Power - Generation/RT_5V -> /Project Architecture/Interface - Interconnects/POS_SENSOR_MOSI
- U1 pad 5: /Project Architecture/Power - Generation/FB_5V -> GND
- U1 pad 6: /Project Architecture/Power - Generation/PG_5V -> unconnected-(U1-B-Pad6)
- U1 pad 7: Net-(U1-BOOT) -> unconnected-(U1-A-Pad7)
- U1 pad 8: /Project Architecture/Power - Generation/SW_5V -> unconnected-(U1-W/PWM-Pad8)
- U1 pad 9: GND -> unconnected-(U1-V-Pad9)
- U3 pad 2: +5V -> +VPROT
- U3 pad 3: /Project Architecture/Power - Generation/PG_5V -> +VPROT
- U3 pad 4: GND -> /Project Architecture/Power - Generation/PG_5V
- U3 pad 5: /Project Architecture/Power - Generation/FB_3V3 -> /Project Architecture/Power - Generation/FB_5V
- U3 pad 6: +3V3 -> Net-(U3-VCC)
- U3 pad 7: /Project Architecture/Power - Generation/SW_3V3 -> Net-(U3-BOOT)
- U3 pad 8: unconnected-(U3-PG-Pad8) -> /Project Architecture/Power - Generation/SW_5V
- U6 pad 24: +A3V3 -> +3V3
- U6 pad 4: +VBAT -> +VPROT
- U6 pad 5: +VBAT -> +VPROT
- U7 pad 1: /Project Architecture/Interface - Interconnects/D+ -> +3V3
- U7 pad 2: /Project Architecture/Interface - Interconnects/D- -> unconnected-(U7-NC-Pad2)
- U7 pad 4: /Project Architecture/Interface - USB to UART/RTS -> /Project Architecture/Power - Generation/PG_5V
- U7 pad 5: /Project Architecture/Interface - USB to UART/CTS -> unconnected-(U7-NC-Pad5)
- U7 pad 6: /Project Architecture/Interface - USB to UART/DTR -> +5V
- U7 pad 7: +5V_USB -> GND
- U8 pad 3: +3V3 -> +5V
- U8 pad 5: +5V -> +3V3
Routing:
- net +A3V3: track 121.5 -> 0.00 mm, vias 5 -> 0
- net +VBAT: track 91.6 -> 0.00 mm, vias 337 -> 0
- net +VPROT: track 0.00 -> 84.1 mm, vias 0 -> 48
- net /Project Architecture/MCU - IOs/VBAT_SENSE: track 86.1 -> 13.2 mm, vias 1 -> 0
- net /Project Architecture/Interface - Interconnects/POS_SENSOR_CS: track 84.8 -> 16.2 mm, vias 2 -> 1
- net /Project Architecture/MCU - IOs/DRV_ENABLE: track 23.3 -> 80.1 mm, vias 2 -> 4
- net CHASSIS3: track 0.00 -> 45.6 mm
- net /Project Architecture/Power - Generation/PG_5V: track 59.7 -> 15.6 mm
- net +5V: track 57.5 -> 16.2 mm, vias 13 -> 8
- net /Project Architecture/USER - LEDs/PWR_LED_D: track 37.0 -> 0.00 mm, vias 2 -> 0
- net /Project Architecture/MCU - IOs/DRV_MISO: track 21.7 -> 58.5 mm, vias 0 -> 2
- net /Project Architecture/Interface - Interconnects/NRST: track 18.5 -> 54.5 mm, vias 0 -> 1
- net /Project Architecture/Interface - Interconnects/I2C3_SCL: track 0.00 -> 35.1 mm, vias 0 -> 2
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- added copper zone on B.Cu, net +VPROT
- added copper zone on F.Cu, net +VPROT
- added copper zone on In2.Cu, net +VPROT
- added copper zone on In3.Cu, net +VPROT
- removed copper zone on In3.Cu, net +3V3
- removed copper zone on In3.Cu, net +5V
- removed copper zone on F.Cu, net +A3V3
- removed copper zone on B.Cu, net +VBAT
- removed copper zone on F.Cu, net +VBAT
- removed copper zone on In2.Cu, net +VBAT
- removed copper zone on In3.Cu, net +VBAT
- removed copper zone on B.Cu, net /Project Architecture/MCU - IOs/TEMP_SENSE
- removed copper zone on B.Cu, net CHASSIS
- removed copper zone on F.Cu, net CHASSIS
- removed copper zone on In1.Cu, net CHASSIS
- removed copper zone on In2.Cu, net CHASSIS
- removed copper zone on In3.Cu, net CHASSIS
- removed copper zone on In4.Cu, net CHASSIS
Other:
- board size 80 x 93.5 mm -> 70 x 70 mm
- board text added: "10k NTC"
- board text added: "3V3"
- board text added: "AS5047 (AUX)"
- board text added: "CAN"
- board text added: "CANH"
- board text added: "CANL"
- board text added: "ESTOP"
- board text added: "GND"
- board text added: "I2C"
- board text added: "MCU"
- board text added: "MOTOR TEMP"
- board text added: "NRST"
- board text added: "SWCLK"
- board text added: "SWDIO"
- board text added: "UART"
- board text removed: "AUX ENCODER"
- board text removed: "DBG"
- board text removed: "DRV8323"
- board text removed: "FDCAN"
- board text removed: "FDCAN TERM"
- board text removed: "MOTOR CONTROLLER AUG 2026"
- board text removed: "OFF"
- board text removed: "ON"
- board text removed: "STM32F431"
- board text removed: "TEMP"
- board text removed: "USB - SERIAL"
